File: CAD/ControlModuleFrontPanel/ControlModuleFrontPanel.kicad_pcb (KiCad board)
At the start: 2 copper layers, 243.8 x 95.2 mm, 13 parts

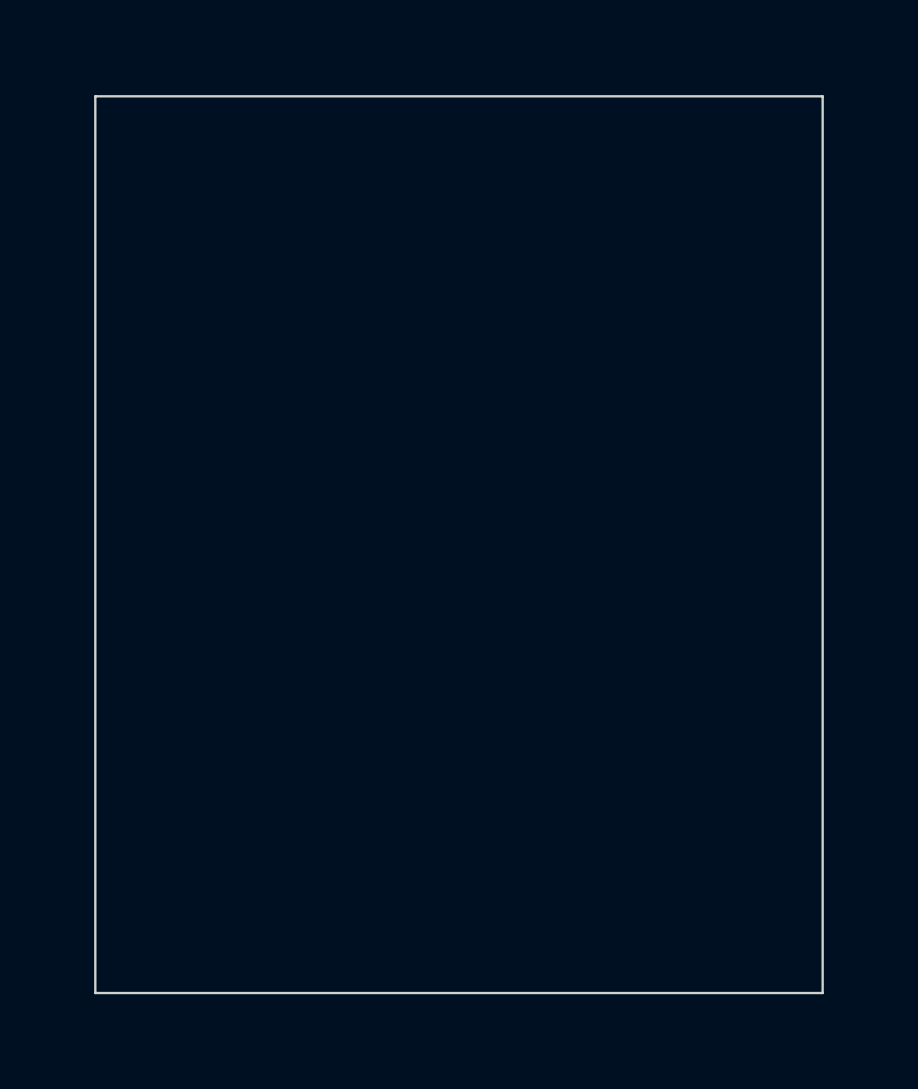
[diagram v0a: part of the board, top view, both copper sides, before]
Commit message: updated power supply and front panel
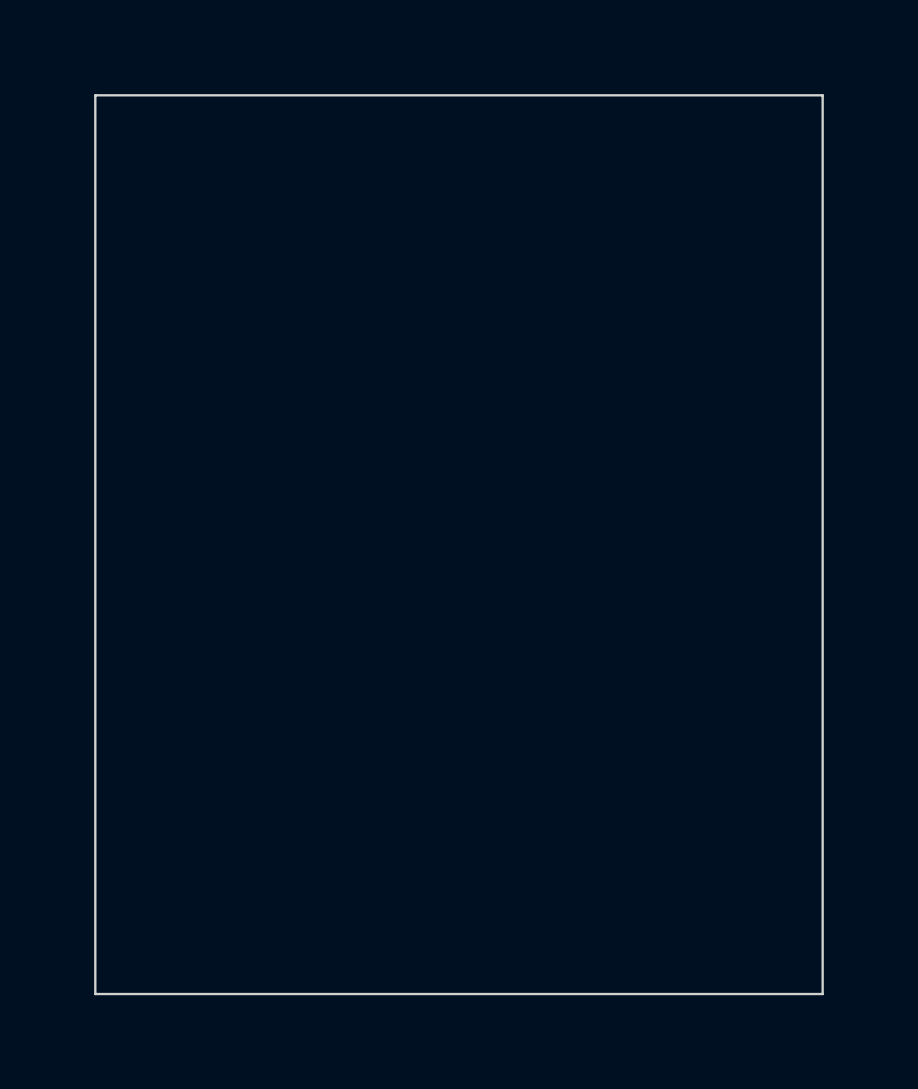
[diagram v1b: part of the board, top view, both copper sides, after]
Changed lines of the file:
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@@
-(kicad_pcb (version 20171130) (host pcbnew "(5.1.2-1)-1")
+(kicad_pcb (version 20171130) (host pcbnew "(5.1.2)-2")
   (general
     (thickness 1.6)
@@
   (gr_line (start 185.674 110.871) (end 129.413 110.871) (layer Edge.Cuts) (width 0.15))
   (gr_line (start 72.3646 61.3156) (end 72.3646 58.674) (layer Dwgs.User) (width 0.15))
-  (gr_line (start 104.4575 113.0935) (end 104.4575 55.9435) (layer Edge.Cuts) (width 0.15))
+  (gr_line (start 104.4575 113.157) (end 104.4575 55.88) (layer Edge.Cuts) (width 0.15))
   (gr_line (start 90.2462 61.3156) (end 72.3646 61.3156) (layer Dwgs.User) (width 0.15))
-  (gr_line (start 58.1025 113.0935) (end 104.4575 113.0935) (layer Edge.Cuts) (width 0.15))
+  (gr_line (start 58.1025 113.157) (end 104.4575 113.157) (layer Edge.Cuts) (width 0.15))
   (gr_line (start 72.3646 58.674) (end 90.2462 58.674) (layer Dwgs.User) (width 0.15))
-  (gr_line (start 58.1025 55.9435) (end 104.4575 55.9435) (layer Edge.Cuts) (width 0.15))
-  (gr_line (start 58.1025 113.0935) (end 58.1025 55.9435) (layer Edge.Cuts) (width 0.15))
+  (gr_line (start 58.1025 55.88) (end 104.4575 55.88) (layer Edge.Cuts) (width 0.15))
+  (gr_line (start 58.1025 113.157) (end 58.1025 55.88) (layer Edge.Cuts) (width 0.15))
   (gr_line (start 58.166 59.944) (end 104.394 59.944) (layer Dwgs.User) (width 0.15))
   (gr_line (start 81.3054 61.7982) (end 81.3054 57.023) (layer Dwgs.User) (width 0.15))
